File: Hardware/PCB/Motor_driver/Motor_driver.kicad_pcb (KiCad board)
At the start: 4 copper layers, 60 x 60 mm, 92 parts, among them J4 Conn_ST_STDC14, U3 STM32L412KBTx, U4 USBLC6-2SC6

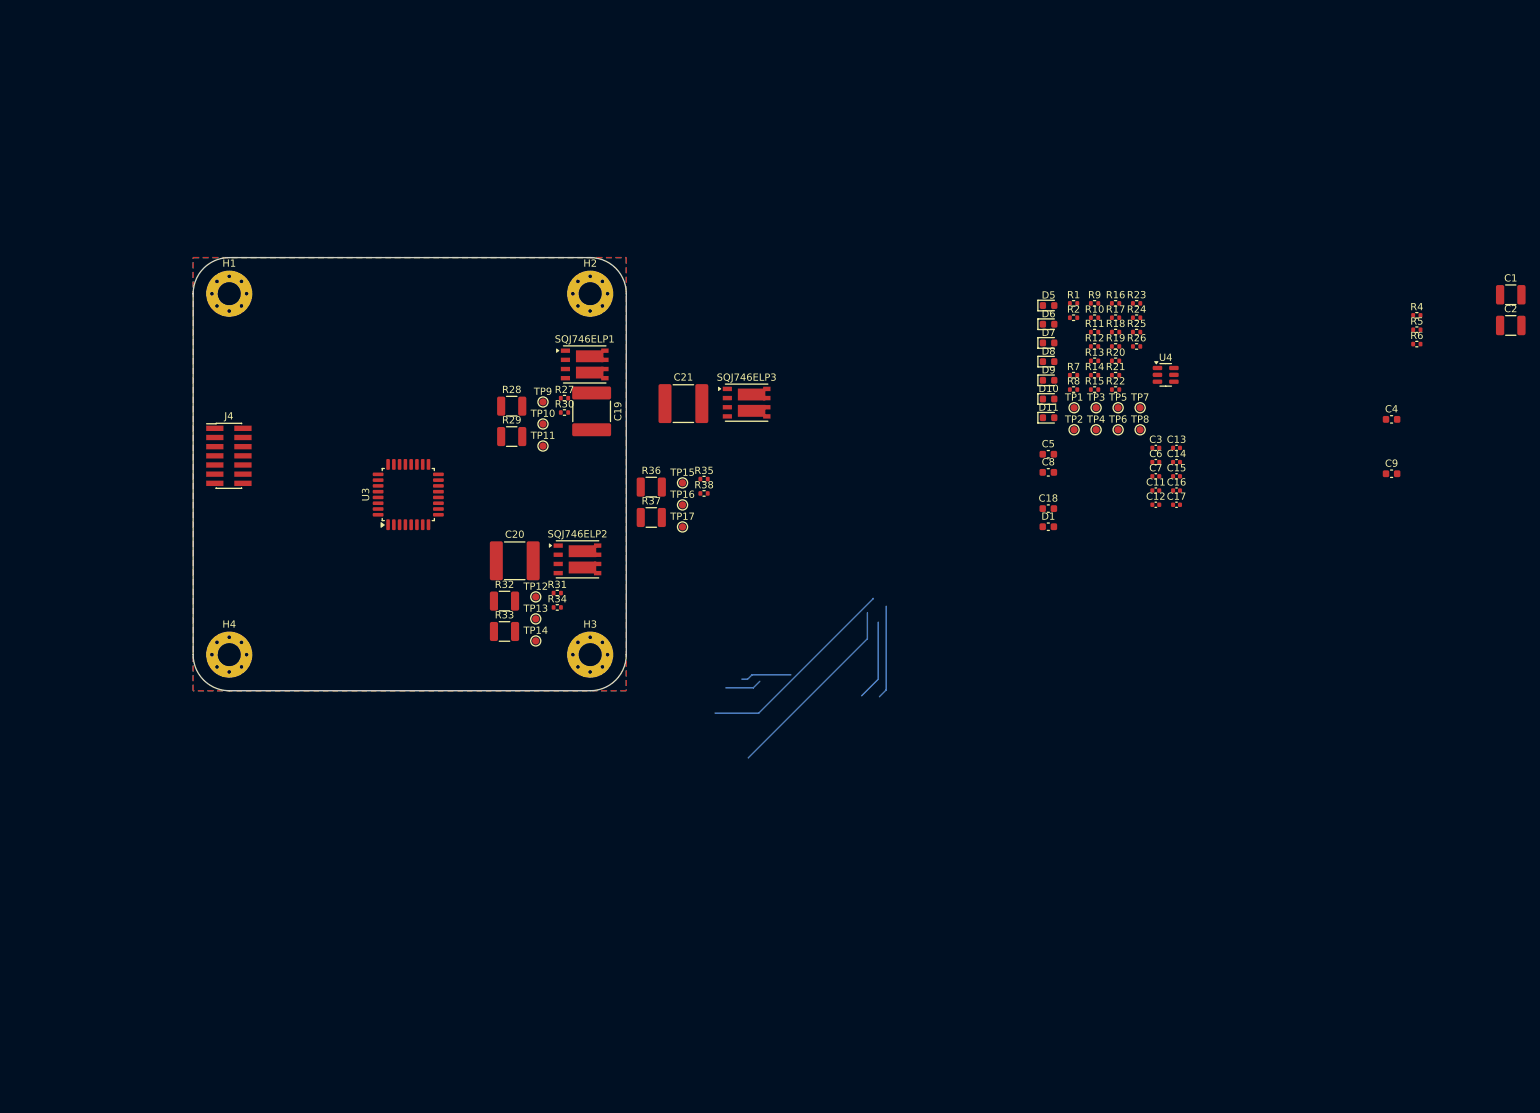
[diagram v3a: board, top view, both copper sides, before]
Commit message: Pcb moteur routé
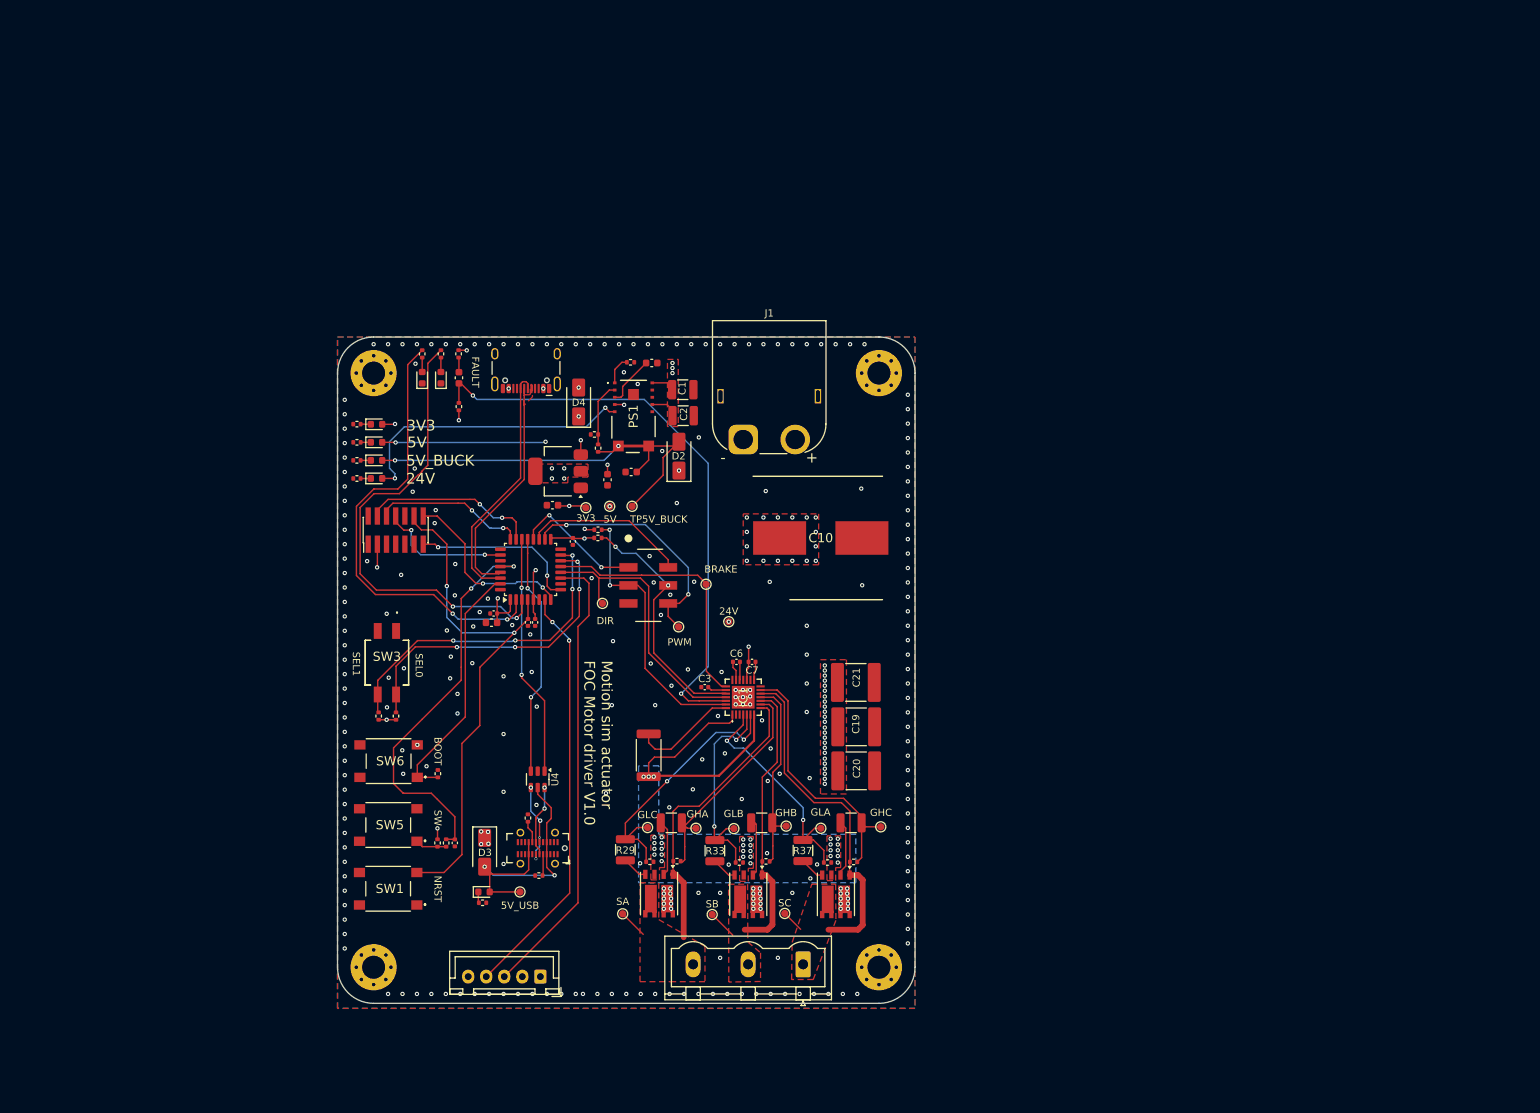
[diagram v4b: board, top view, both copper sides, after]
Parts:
- removed C11, C13: 10n, Capacitor_SMD:C_0402_1005Metric
- removed R12, R13, R16, R17: 10k, Resistor_SMD:R_0402_1005Metric
- removed TP1: 24V, TestPoint:TestPoint_Pad_D1.0mm
- removed TP10, TP12, TP13, TP14, TP15, TP16, TP17: GATE C, TestPoint:TestPoint_Pad_D1.0mm
- removed TP2: 5V_BUCK, TestPoint:TestPoint_Pad_D1.0mm
- removed TP3: 5V_USB, TestPoint:TestPoint_Pad_D1.0mm
- removed TP4: 5V, TestPoint:TestPoint_Pad_D1.0mm
- removed TP5: 3V3, TestPoint:TestPoint_Pad_D1.0mm
- removed TP6: PWM, TestPoint:TestPoint_Pad_D1.0mm
- removed TP7: DIR, TestPoint:TestPoint_Pad_D1.0mm
- removed TP8: BRAKE, TestPoint:TestPoint_Pad_D1.0mm
- added 24V: 24V, TestPoint:TestPoint_Pad_D1.0mm, F.Cu at (119.2, 95.4)
- added 3V3: 3V3, TestPoint:TestPoint_Pad_D1.0mm, F.Cu at (99.4, 79.7)
- added 5V: 5V, TestPoint:TestPoint_Pad_D1.0mm, F.Cu at (102.7, 79.5)
- added 5V_USB: 5V_USB, TestPoint:TestPoint_Pad_D1.0mm, F.Cu at (90.3, 132.9)
- added BRAKE: BRAKE, TestPoint:TestPoint_Pad_D1.0mm, F.Cu at (116.0, 90.2)
- added C10: 470u, SamacSys_Parts:CAPAE1710X1700N, F.Cu at (131.9, 83.8)
- added D2: FSV340AF, Diode_SMD:D_SMA, F.Cu at (112.3, 72.5)
- added D3: FSV340AF, Diode_SMD:D_SMA, F.Cu at (85.4, 127.4)
- added D4: FSV340AF, Diode_SMD:D_SMA, F.Cu at (98.4, 65.0)
- added DIR: DIR, TestPoint:TestPoint_Pad_D1.0mm, F.Cu at (101.7, 92.9)
- added G***: LOGO, LOGO, B.Cu at (107.0, 101.0)
- added GHB: GATE C, TestPoint:TestPoint_Pad_D1.0mm, F.Cu at (127.2, 123.8)
- added GHC: GATE C, TestPoint:TestPoint_Pad_D1.0mm, F.Cu at (140.2, 123.8)
- added GLA: GATE C, TestPoint:TestPoint_Pad_D1.0mm, F.Cu at (131.9, 124.0)
- added GLB: GATE C, TestPoint:TestPoint_Pad_D1.0mm, F.Cu at (119.9, 124.1)
- added IC1: A89307KETSR-J, SamacSys_Parts:A8519KETTRR1, F.Cu at (121.2, 105.9)
- added J1: Conn_01x02, Connector_AMASS:AMASS_XT60PW-M_1x02_P7.20mm_Horizontal, F.Cu at (121.2, 70.2)
- added J2: Conn_01x05, Connector_JST:JST_XH_B5B-XH-A_1x05_P2.50mm_Vertical, F.Cu at (93.1, 144.6)
- added J3: Conn_01x03, Connector_Phoenix_GMSTB:PhoenixContact_GMSTBVA_2,5_3-G-7,62_1x03_P7.62mm_Vertical, F.Cu at (129.5, 142.9)
- added J5: USB_C_Receptacle_USB2.0_16P, Connector_USB:USB_C_Receptacle_HCTL_HC-TYPE-C-16P-01A, F.Cu at (91.1, 59.4)
- added J6: 629712010214, Connector_USB:USB_C_Receptacle_GCT_USB4115-03-C, F.Cu at (92.7, 126.8)
- added PS1: 171013801, SamacSys_Parts:171013801, F.Cu at (106.0, 67.0)
- added PWM: PWM, TestPoint:TestPoint_Pad_D1.0mm, F.Cu at (112.2, 96.2)
- added R3: 2m, Resistor_SMD:R_2512_6332Metric, F.Cu at (108.1, 113.9)
- added SA: GATE C, TestPoint:TestPoint_Pad_D1.0mm, F.Cu at (104.5, 135.9)
- added SB: GATE C, TestPoint:TestPoint_Pad_D1.0mm, F.Cu at (116.9, 136.0)
- added SC: GATE C, TestPoint:TestPoint_Pad_D1.0mm, F.Cu at (127.0, 135.8)
- added SW1: SW_Push, SamacSys_Parts:430152043826, F.Cu at (72.0, 132.4)
- added SW3: SW_DIP_x02, SamacSys_Parts:418121270802, F.Cu at (71.8, 101.1)
- added SW5: SW_Push, SamacSys_Parts:430152043826, F.Cu at (72.0, 123.6)
- added SW6: SW_Push, SamacSys_Parts:430152043826, F.Cu at (72.1, 114.8)
- added TP5V_BUCK: 5V_BUCK, TestPoint:TestPoint_Pad_D1.0mm, F.Cu at (105.8, 79.5)
- added U1: AZ1117-3.3, Package_TO_SOT_SMD:SOT-223, F.Cu at (95.6, 74.6)
- added U2: ~, Custom:452406020024, F.Cu at (111.3, 88.4)
- J4: value Conn_ST_STDC14 -> 629722000214
- moved H1 129.6 mm to (140.0, 143.3)
- moved R9 118.7 mm to (85.1, 134.4)
- moved R18 116.7 mm to (80.0, 126.1), turned to -90 degrees
- moved R19 116.4 mm to (78.8, 126.1), turned to 90 degrees
- moved C1 115.4 mm to (112.8, 63.3)
- moved C2 115.3 mm to (112.9, 66.9)
- moved R6 114.6 mm to (100.6, 69.5), turned to 180 degrees
- moved R5 114.6 mm to (101.1, 71.4), turned to 90 degrees
- moved C14 113.0 mm to (81.2, 126.1), turned to -90 degrees
- moved R14 109.8 mm to (70.7, 108.5), turned to -90 degrees
- moved R4 109.1 mm to (105.6, 59.5)
- moved D7 109.1 mm to (85.3, 132.9)
- moved R22 107.9 mm to (78.9, 116.5), turned to -90 degrees
- moved R20 107.1 mm to (92.9, 130.6)
- moved R15 106.8 mm to (73.1, 108.5), turned to -90 degrees
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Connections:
- R23 pad 1: /SCL_I2C1 -> /FG
- R24 pad 1: /SDA_I2C1 -> /SPD
- R27 pad 2: /arm_bridge_A/Sx -> /SA
- R31 pad 2: /arm_bridge_B/Sx -> /SB
- R35 pad 2: /arm_bridge_C/Sx -> /SC
- SQJ746ELP1 pad 1: /arm_bridge_A/Sx -> /SA
- SQJ746ELP1 pad 5: /arm_bridge_A/Sx -> +24V
- SQJ746ELP1 pad 6: +24V -> /SA
- SQJ746ELP2 pad 1: /arm_bridge_B/Sx -> /SB
- SQJ746ELP2 pad 5: /arm_bridge_B/Sx -> +24V
- SQJ746ELP2 pad 6: +24V -> /SB
- SQJ746ELP3 pad 1: /arm_bridge_C/Sx -> /SC
- SQJ746ELP3 pad 5: /arm_bridge_C/Sx -> +24V
- SQJ746ELP3 pad 6: +24V -> /SC
- U3 pad 25: /BTN_1 -> unconnected-(U3-PA15-Pad25)
- U3 pad 27: /BTN_2 -> unconnected-(U3-PB4-Pad27)
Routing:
- net Net-(D1-K): track 0.00 -> 81.9 mm, vias 0 -> 2
- net /NRST: track 0.00 -> 73.5 mm, vias 0 -> 2
- net /LED_1: track 0.00 -> 64.8 mm, vias 0 -> 2
- net /LED_0: track 0.00 -> 63.8 mm, vias 0 -> 2
- net /ENC_A: track 0.00 -> 63.6 mm
- net /5V_BUCK: track 0.00 -> 61.2 mm, vias 0 -> 2
- net /ENC_B: track 0.00 -> 58.4 mm, vias 0 -> 2
- net /BTN_3: track 0.00 -> 55.2 mm, vias 0 -> 2
- net +24V: track 0.00 -> 52.5 mm, vias 0 -> 78
- net /SC: track 0.00 -> 50.2 mm
- net /ADD_SEL_1: track 0.00 -> 45.4 mm, vias 0 -> 4
- net /SA: track 0.00 -> 44.9 mm
- net /ADD_SEL_0: track 0.00 -> 44.7 mm, vias 0 -> 4
- net /SB: track 0.00 -> 43.0 mm
- net /5V_USB: track 0.00 -> 42.4 mm, vias 0 -> 2
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- added copper zone on F.Cu, net +24V
- added copper zone on F.Cu, net +3.3V
- added copper zone on In2.Cu, net /5V_Cmd
- added copper zone on F.Cu, net /Cmd_TX
- added copper zone on B.Cu, net /LSS
- added copper zone on F.Cu, net /LSS
- added copper zone on F.Cu, net /SA
- added copper zone on F.Cu, net /SB
- added copper zone on F.Cu, net /SC
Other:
- board size 60 x 60 mm -> 80 x 92.3 mm
- board text added: "24V"
- board text added: "3V3"
- board text added: "5V"
- board text added: "5V_BUCK"
- board text added: "BOOT"
- board text added: "FAULT"
- board text added: "GHA"
- board text added: "GLC"
- board text added: "Motion sim actuator FOC Motor driver V1.0"
- board text added: "NRST"
- board text added: "SEL0"
- board text added: "SEL1"
- board text added: "SW"

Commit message: Gerber
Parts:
- C19, C20, C21: moved to B.Cu
- R3: footprint Resistor_SMD:R_2512_6332Metric -> Resistor_SMD:R_Shunt_Ohmite_LVK24
- moved C21 38.3 mm to (113.2, 134.0)
- moved C19 26.7 mm to (125.7, 134.2)
- moved C20 18.2 mm to (137.8, 134.3)
- moved C2 10.9 mm to (102.0, 67.9), turned to -90 degrees
- moved R5 10.9 mm to (105.9, 61.6), turned to 0 degrees
- moved R6 10.4 mm to (105.9, 60.6)
- moved C1 8.82 mm to (105.3, 67.9), turned to -90 degrees
- moved C9 8.64 mm to (113.5, 71.1), turned to 0 degrees
- moved PS1 5.73 mm to (111.0, 64.2)
- moved C4 4.60 mm to (105.3, 62.9), turned to 180 degrees
- moved D2 3.76 mm to (109.9, 75.4)
- moved SC 3.02 mm to (129.6, 137.3)
- moved R3 1.46 mm to (106.8, 113.4), turned to 180 degrees
- moved SB 1.12 mm to (117.9, 135.5)
- moved R4 0.33 mm to (105.9, 59.6), turned to 180 degrees
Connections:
- IC1 pad 1: /LSS -> Net-(IC1-SENP)
- IC1 pad 28: GND -> Net-(IC1-SENN)
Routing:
- net Net-(IC1-SENP): track 0.00 -> 19.0 mm
- net Net-(IC1-SENN): track 0.00 -> 17.6 mm
- net /LSS: track 36.5 -> 21.8 mm, vias 30 -> 35
- net GND: track 14.7 -> 0.00 mm, vias 238 -> 275
- net +24V: track 52.5 -> 42.7 mm, vias 78 -> 59
- net /5V_BUCK: track 61.2 -> 68.2 mm
- net Net-(PS1-FB): track 8.92 -> 3.01 mm
- net Net-(PS1-VCC): track 7.05 -> 2.86 mm
- net Net-(PS1-FSW): track 3.94 -> 2.01 mm
- net /SB: track 43.0 -> 41.9 mm
- net +3.3V: track 37.0 -> 36.4 mm, vias 16 -> 19
